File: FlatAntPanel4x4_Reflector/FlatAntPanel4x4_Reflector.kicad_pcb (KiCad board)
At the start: 2 copper layers, 186 x 226 mm, 6 parts

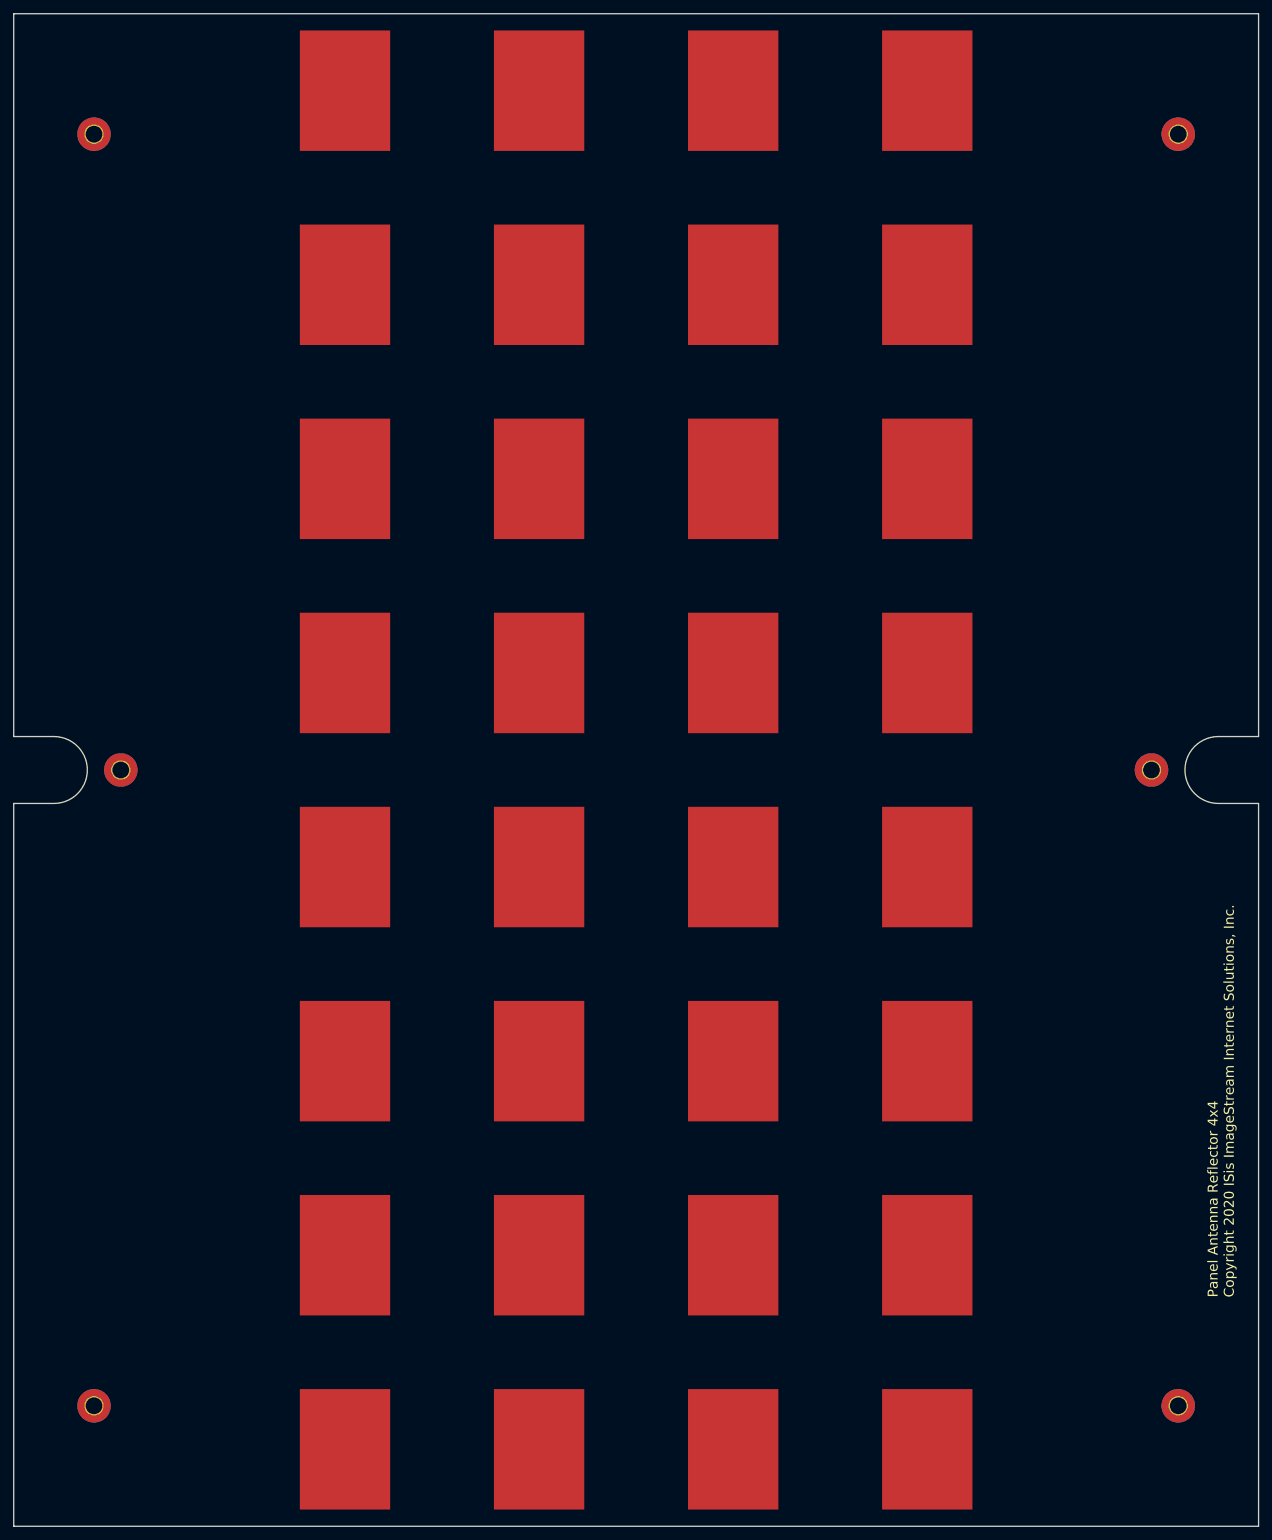
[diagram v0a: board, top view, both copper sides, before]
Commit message: Finalize 4x4 flat ant and director. Start dual polarity 4x4 antenna
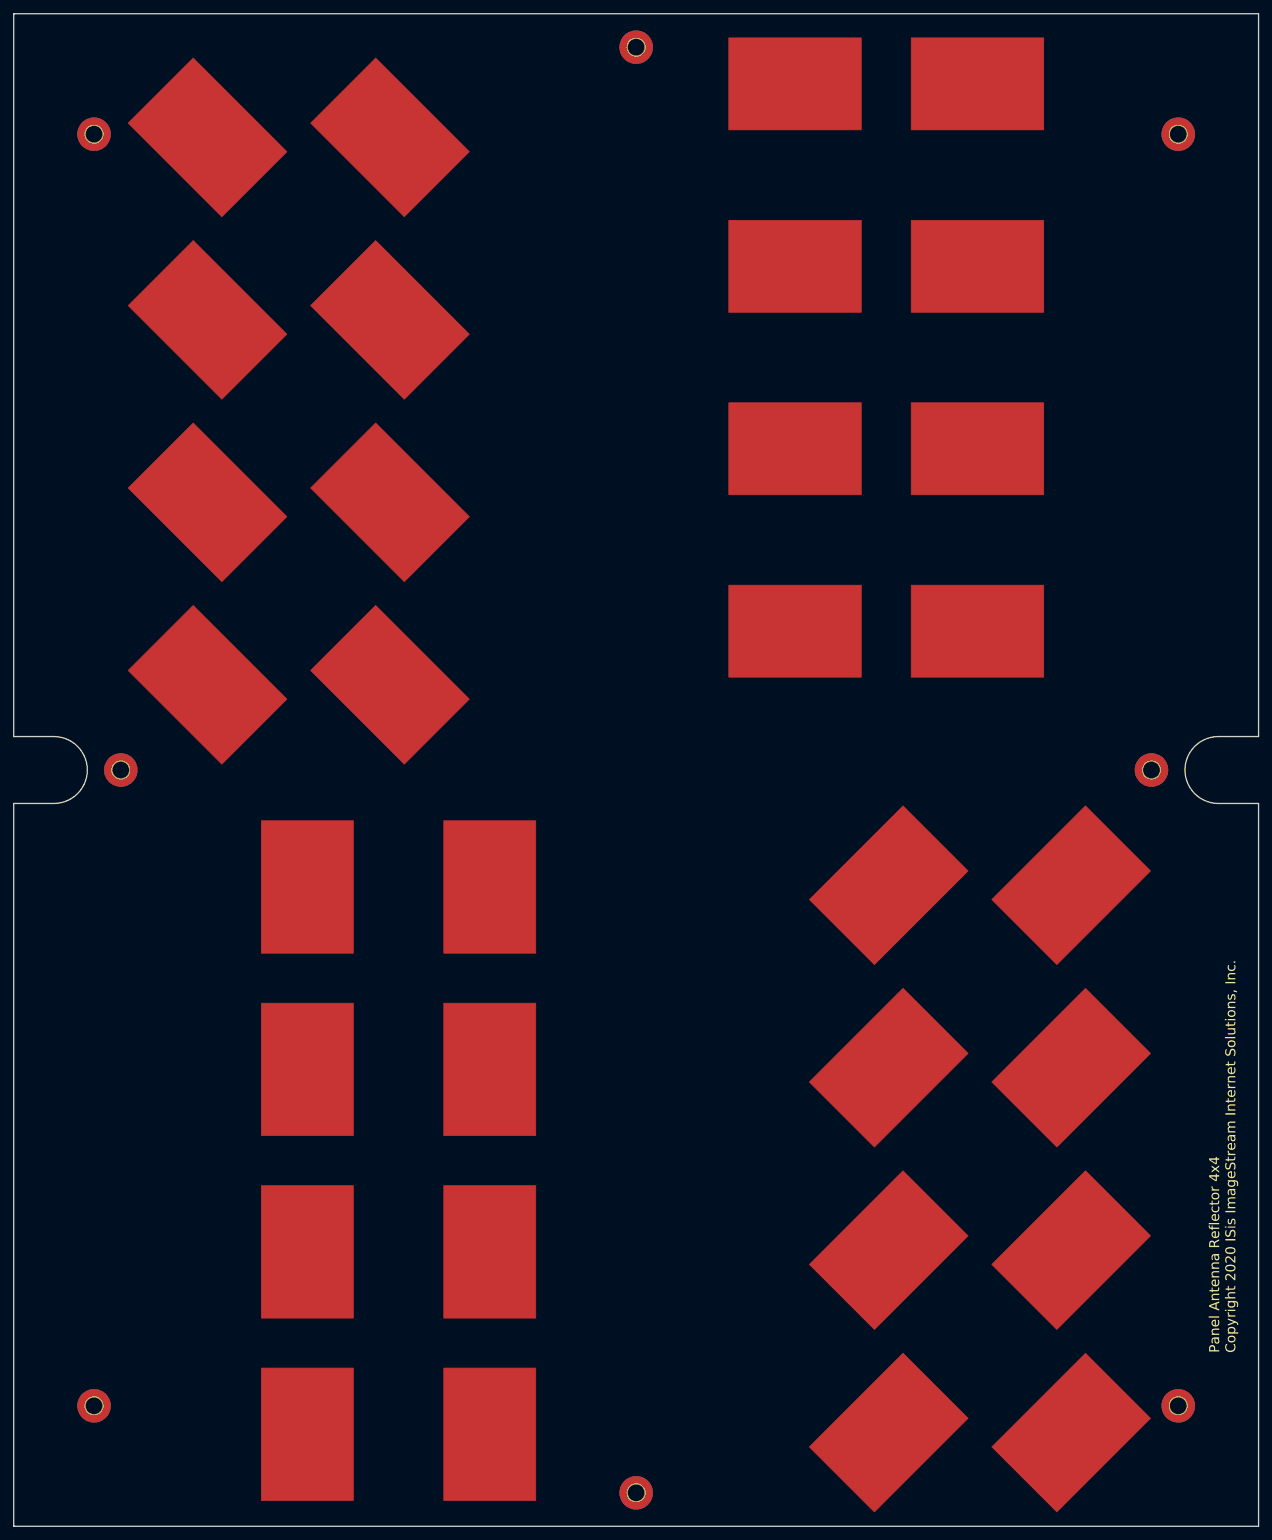
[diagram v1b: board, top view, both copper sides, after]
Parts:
- added H10: Mounting Hole, MountingHole:MountingHole_2.5mm_Pad_TopBottom, F.Cu at (93.0, 5.00)
- added H9: Mounting Hole, MountingHole:MountingHole_2.5mm_Pad_TopBottom, F.Cu at (93.0, 221.0)
- added REF**: Patch_Reflector_10_pct, Scott-RF-JLCPCB-1.2mm7628-4layer:Patch_Reflector_10_pct, F.Cu at (29.0, 100.3)
- added REF**: Patch_Reflector_10_pct, Scott-RF-JLCPCB-1.2mm7628-4layer:Patch_Reflector_10_pct, F.Cu at (130.7, 157.5)
- added REF**: Patch_Reflector_10_pct, Scott-RF-JLCPCB-1.2mm7628-4layer:Patch_Reflector_10_pct, F.Cu at (29.0, 18.5)
- added REF**: Patch_Reflector_10_pct, Scott-RF-JLCPCB-1.2mm7628-4layer:Patch_Reflector_10_pct, F.Cu at (116.7, 65.0)
- added REF**: Patch_Reflector_10_pct, Scott-RF-JLCPCB-1.2mm7628-4layer:Patch_Reflector_10_pct, F.Cu at (56.2, 18.5)
- added REF**: Patch_Reflector_10_pct, Scott-RF-JLCPCB-1.2mm7628-4layer:Patch_Reflector_10_pct, F.Cu at (29.0, 45.8)
- added REF**: Patch_Reflector_10_pct, Scott-RF-JLCPCB-1.2mm7628-4layer:Patch_Reflector_10_pct, F.Cu at (116.7, 92.3)
- added REF**: Patch_Reflector_10_pct, Scott-RF-JLCPCB-1.2mm7628-4layer:Patch_Reflector_10_pct, F.Cu at (71.1, 185.0)
- added REF**: Patch_Reflector_10_pct, Scott-RF-JLCPCB-1.2mm7628-4layer:Patch_Reflector_10_pct, F.Cu at (43.9, 212.3)
- added REF**: Patch_Reflector_10_pct, Scott-RF-JLCPCB-1.2mm7628-4layer:Patch_Reflector_10_pct, F.Cu at (56.2, 45.8)
- added REF**: Patch_Reflector_10_pct, Scott-RF-JLCPCB-1.2mm7628-4layer:Patch_Reflector_10_pct, F.Cu at (116.7, 10.5)
- added REF**: Patch_Reflector_10_pct, Scott-RF-JLCPCB-1.2mm7628-4layer:Patch_Reflector_10_pct, F.Cu at (130.7, 212.0)
- added REF**: Patch_Reflector_10_pct, Scott-RF-JLCPCB-1.2mm7628-4layer:Patch_Reflector_10_pct, F.Cu at (43.9, 130.5)
- added REF**: Patch_Reflector_10_pct, Scott-RF-JLCPCB-1.2mm7628-4layer:Patch_Reflector_10_pct, F.Cu at (71.1, 130.5)
- added REF**: Patch_Reflector_10_pct, Scott-RF-JLCPCB-1.2mm7628-4layer:Patch_Reflector_10_pct, F.Cu at (158.0, 130.2)
- added REF**: Patch_Reflector_10_pct, Scott-RF-JLCPCB-1.2mm7628-4layer:Patch_Reflector_10_pct, F.Cu at (158.0, 157.5)
- added REF**: Patch_Reflector_10_pct, Scott-RF-JLCPCB-1.2mm7628-4layer:Patch_Reflector_10_pct, F.Cu at (158.0, 212.0)
- added REF**: Patch_Reflector_10_pct, Scott-RF-JLCPCB-1.2mm7628-4layer:Patch_Reflector_10_pct, F.Cu at (29.0, 73.0)
- added REF**: Patch_Reflector_10_pct, Scott-RF-JLCPCB-1.2mm7628-4layer:Patch_Reflector_10_pct, F.Cu at (56.2, 73.0)
- added REF**: Patch_Reflector_10_pct, Scott-RF-JLCPCB-1.2mm7628-4layer:Patch_Reflector_10_pct, F.Cu at (144.0, 92.3)
- added REF**: Patch_Reflector_10_pct, Scott-RF-JLCPCB-1.2mm7628-4layer:Patch_Reflector_10_pct, F.Cu at (43.9, 185.0)
- added REF**: Patch_Reflector_10_pct, Scott-RF-JLCPCB-1.2mm7628-4layer:Patch_Reflector_10_pct, F.Cu at (144.0, 10.5)
- added REF**: Patch_Reflector_10_pct, Scott-RF-JLCPCB-1.2mm7628-4layer:Patch_Reflector_10_pct, F.Cu at (71.1, 157.7)
- added REF**: Patch_Reflector_10_pct, Scott-RF-JLCPCB-1.2mm7628-4layer:Patch_Reflector_10_pct, F.Cu at (158.0, 184.7)
- added REF**: Patch_Reflector_10_pct, Scott-RF-JLCPCB-1.2mm7628-4layer:Patch_Reflector_10_pct, F.Cu at (43.9, 157.7)
- added REF**: Patch_Reflector_10_pct, Scott-RF-JLCPCB-1.2mm7628-4layer:Patch_Reflector_10_pct, F.Cu at (130.7, 184.7)
- added REF**: Patch_Reflector_10_pct, Scott-RF-JLCPCB-1.2mm7628-4layer:Patch_Reflector_10_pct, F.Cu at (130.7, 130.2)
- added REF**: Patch_Reflector_10_pct, Scott-RF-JLCPCB-1.2mm7628-4layer:Patch_Reflector_10_pct, F.Cu at (144.0, 37.7)
- added REF**: Patch_Reflector_10_pct, Scott-RF-JLCPCB-1.2mm7628-4layer:Patch_Reflector_10_pct, F.Cu at (71.1, 212.3)
- added REF**: Patch_Reflector_10_pct, Scott-RF-JLCPCB-1.2mm7628-4layer:Patch_Reflector_10_pct, F.Cu at (56.2, 100.3)
- added REF**: Patch_Reflector_10_pct, Scott-RF-JLCPCB-1.2mm7628-4layer:Patch_Reflector_10_pct, F.Cu at (144.0, 65.0)
- added REF**: Patch_Reflector_10_pct, Scott-RF-JLCPCB-1.2mm7628-4layer:Patch_Reflector_10_pct, F.Cu at (116.7, 37.7)
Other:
- board text added: "FR4 0.6mm"
